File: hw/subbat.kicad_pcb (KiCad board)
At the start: 2 copper layers, 100 x 100 mm, 247 parts, among them J1 Conn_01x02, J10 Conn_01x06_Male, J11 USB_Ax2, J12 USB_Ax2, J13 USB_Ax2, J14 RJ45, J15 Conn_01x04_Male, J16 Conn_01x06_Male, J17 Conn_01x06_Male, J18 Conn_01x02, J19 USB_B_Micro, J2 Conn_01x02, J20 Conn_02x08_Odd_Even, J21 Conn_01x02, J24 Conn_01x02, J3 Conn_01x02, J4 Conn_01x02, J5 Conn_01x02, J6 Conn_01x02, J7 Conn_01x06_Male, J8 Conn_01x02, J9 USB_Ax2, Q1 Q_NPN_BEC, Q10 Q_NPN_BEC, Q11 AOD403, Q12 AOD403, Q13 Q_NPN_BEC, Q14 AOD403, Q15 Q_NPN_BEC, Q16 Q_Photo_NPN_EC, Q17 Q_NPN_BEC, Q18 Q_PNP_BEC, Q2 Q_PMOS_GSD, Q3 TPH11006NL, Q9 AOD403, SW1 SW_Push, SW2 SW_Push, SW3 SW_Push, SW4 SW_SPDT_WITH_SHIELD, SW5 SW_SPDT_WITH_SHIELD, U1 ATMEGA328P-AU, U10 P82B715, U11 TPS54202, U12 L7803, U13 TPS54202, U2 L7803, U3 ATTINY2313-20SU, U4 ATTINY13A-SSU, U5 LT6105, U6 LT6105, U7 LT6105, U8 LT6105, U9 LM393

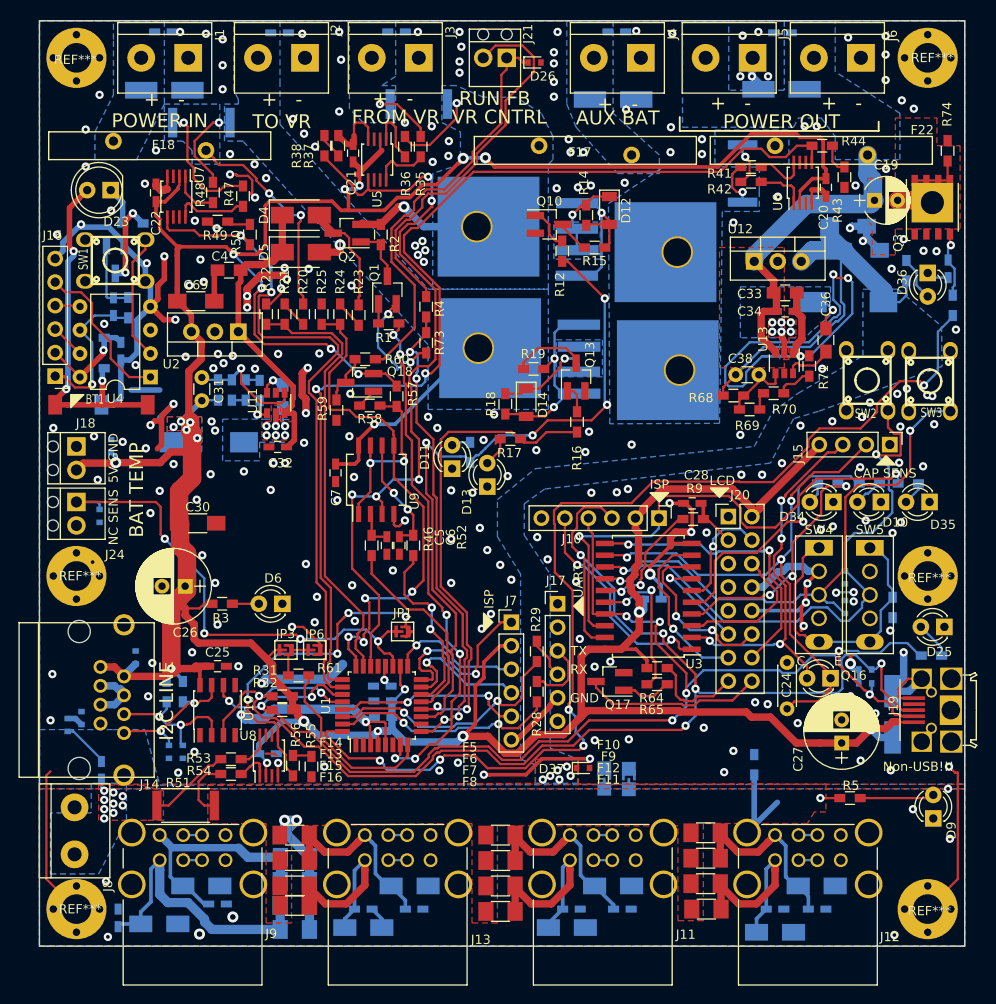
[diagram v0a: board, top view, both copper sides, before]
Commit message: some improvements; DRC clear
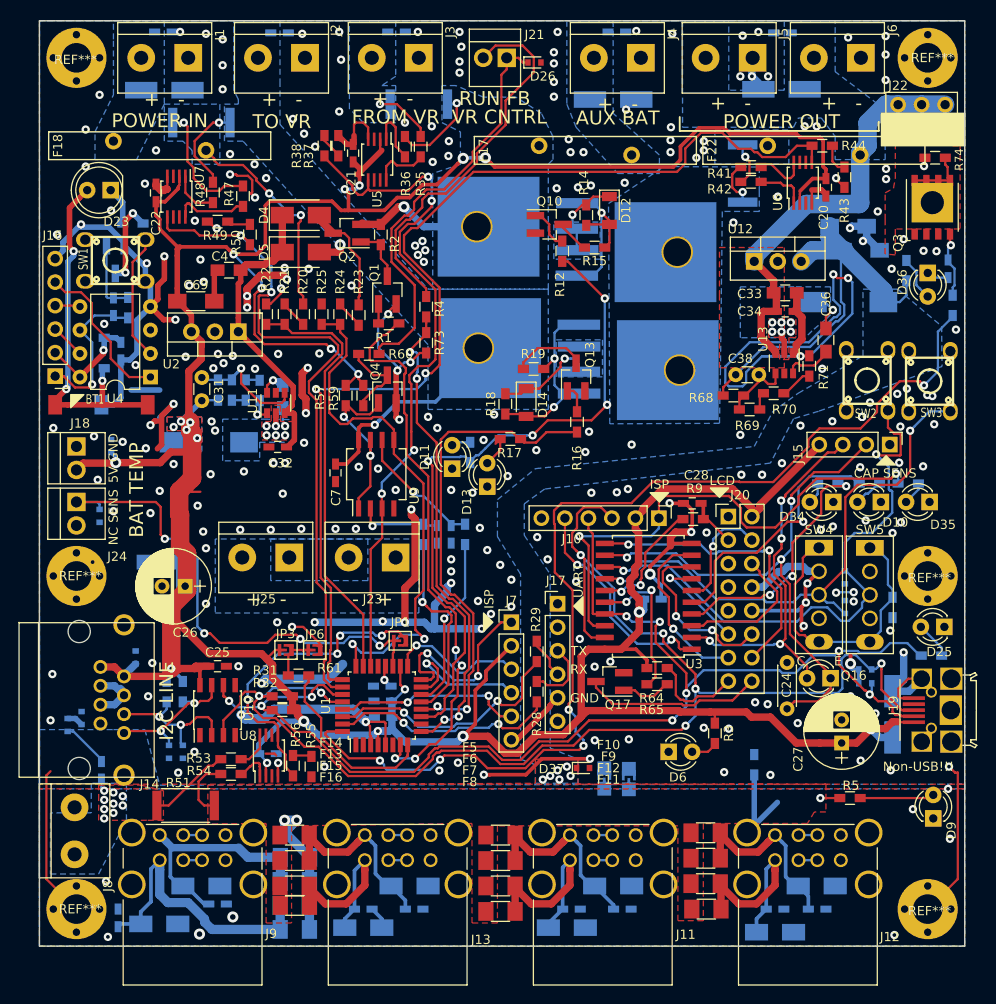
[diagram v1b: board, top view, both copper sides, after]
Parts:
- removed C19: 2200u 35V x 2, Capacitors_ThroughHole:CP_Radial_D5.0mm_P2.50mm
- removed Q18: Q_PNP_BEC, TO_SOT_Packages_SMD:SOT-23_Handsoldering
- removed R58: 10k, Resistors_SMD:R_0603_HandSoldering
- added J22: Conn_02x03_Odd_Even, Pin_Headers:Pin_Header_Straight_2x03_Pitch2.54mm, F.Cu at (112.8, 31.6)
- added J23: Conn_01x02, Terminal_Blocks:TerminalBlock_bornier-2_P5.08mm, F.Cu at (58.5, 78.0)
- added J25: Conn_01x02, Terminal_Blocks:TerminalBlock_bornier-2_P5.08mm, F.Cu at (47.0, 78.0)
- added Q4: Q_NPN_BEC, TO_SOT_Packages_SMD:SOT-23_Handsoldering, F.Cu at (57.6, 59.8)
- C30, C5, C6, R46, R52: moved to B.Cu
- J18, J21, J24: footprint components:TerminalBlock_2_P_2.54mm -> components:TerminalBlock_2_P_2.54mm_without_hole
- R57: value 22k -> 10k
- moved R3 55.1 mm to (93.0, 97.0), turned to 270 degrees
- moved D6 44.7 mm to (88.0, 99.0), turned to 0 degrees
- moved C6 5.72 mm to (64.5, 75.5)
- moved R46 5.72 mm to (61.5, 75.5)
- moved R52 5.72 mm to (66.0, 75.5)
- moved C5 5.58 mm to (63.0, 75.5)
- moved C30 5.53 mm to (33.5, 78.5), turned to 180 degrees
- moved R57 5.50 mm to (53.1, 60.5)
- moved R59 3.30 mm to (55.0, 60.5)
- moved R74 1.54 mm to (116.8, 34.8), turned to 180 degrees
- moved JP1 1.03 mm to (59.0, 87.0)
- moved F22 0.80 mm to (103.7, 34.0)
- moved R60 0.70 mm to (55.6, 56.0)
- moved U9 0.60 mm to (56.4, 69.0)
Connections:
- R59 pad 1: GND -> Net-(Q4-Pad3)
- R59 pad 2: Net-(Q18-Pad3) -> +5V
- R60 pad 1: Net-(Q18-Pad3) -> Net-(Q4-Pad3)
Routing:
- net GND: track 350.8 -> 392.9 mm, vias 247 -> 257
- net /VOUT2: track 33.9 -> 45.6 mm
- net Net-(Q4-Pad3): track 0.00 -> 9.09 mm
- net /ICHARGE_SENS: track 84.1 -> 75.7 mm, vias 5 -> 4
- net Net-(Q18-Pad3): track 5.70 -> 0.00 mm
- net Net-(C5-Pad1): track 4.07 -> 9.14 mm, vias 0 -> 1
- net /~DEEP_SLEEP_EN: track 56.6 -> 61.3 mm, vias 6 -> 4
- net /IUSB_SENS: track 38.7 -> 35.3 mm
- net /IOUT_SENS: track 114.8 -> 117.1 mm
- net Net-(Q18-Pad1): track 2.17 -> 0.00 mm
- net /VA_SENSE_ADC: track 55.2 -> 57.4 mm, vias 4 -> 2
- net /OUTCAP_N: track 12.5 -> 14.6 mm
- net +5V: track 424.3 -> 426.2 mm
- net /SW_BAT: track 74.6 -> 72.8 mm
- net Net-(C6-Pad1): track 12.7 -> 14.3 mm, vias 2 -> 1
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- added copper zone on B.Cu, net /PT_N
- added copper zone on B.Cu, net /PT_P
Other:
- board text added: "- +"

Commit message: Final Revision; PCB ordered using this version
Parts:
- added C19: 1u, Capacitors_SMD:C_0603_HandSoldering, B.Cu at (50.5, 80.8)
- added D33: ESD5Z5.0T1G, Diodes_SMD:D_SOD-523, B.Cu at (30.0, 75.4)
- added D42: ESD5Z5.0T1G, Diodes_SMD:D_SOD-523, B.Cu at (66.1, 24.0)
- added D43: 30V, Diodes_SMD:D_SMA_Handsoldering, B.Cu at (44.6, 74.6)
- added R58: 120R, Resistors_SMD:R_0603_HandSoldering, B.Cu at (27.2, 76.0)
- added R76: 1M, Resistors_SMD:R_0603_HandSoldering, B.Cu at (29.6, 82.4)
- C45: value 1u -> 1u DNI
- D26: moved to B.Cu
- R34, R40: value 2.2k -> 1k
- R74: value 10k -> 10R 2W@long, 20W@1 sec; footprint Resistors_SMD:R_0603_HandSoldering -> Resistors_SMD:R_2512; moved to B.Cu
- R75: value 100k -> 10R
- U10: value P82B715 -> P82B96
- moved J23 11.3 mm to (47.2, 78.0)
- moved J25 11.3 mm to (58.3, 78.0)
- moved D28 1.90 mm to (33.6, 99.0)
- moved R74 1.80 mm to (115.0, 34.8)
- moved D26 1.26 mm to (72.3, 24.1), turned to 270 degrees
- moved D27 1.00 mm to (35.0, 99.0)
- moved R40 0.60 mm to (34.9, 92.5)
- moved R34 0.35 mm to (33.4, 92.5)
- moved C3 0.30 mm to (57.0, 92.2)
- turned R43 to 90 degrees
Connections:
- net Net-(U1-Pad10) renamed /DIGITAL_IN1
- J14 pad 2: GND -> +5V
- J14 pad 6: GND -> +5V
- J14 pad 7: +5V -> GND
- J14 pad 8: +5V -> GND
- J14 pad 9: GND -> Net-(J14-Pad9)
- R57 pad 2: +5V -> /SW_VR
- U1 pad 1: Net-(U1-Pad1) -> /OUTCAP_CHARGE
- U1 pad 11: /SW_BAT -> /DIGITAL_IN0
- U1 pad 2: Net-(U1-Pad2) -> /SW_BAT
- U1 pad 32: /OUTCAP_CHARGE -> /DIGITAL_IN2
- U10 pad 1: (no net) -> SDA
- U10 pad 2: /SCL_L -> /SDA_L
- U10 pad 3: SCL -> /SDA_L
- U10 pad 5: (no net) -> /SCL_L
- U10 pad 6: SDA -> /SCL_L
- U10 pad 7: /SDA_L -> SCL
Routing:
- net GND: track 392.9 -> 484.8 mm, vias 257 -> 298
- net /DIGITAL_IN0: track 0.00 -> 59.3 mm, vias 0 -> 5
- net Net-(J14-Pad9): track 0.00 -> 34.4 mm
- net /ISYS_SENS: track 73.7 -> 85.4 mm
- net /IOUT_SENS: track 117.1 -> 128.6 mm
- net /SW_BAT: track 72.8 -> 83.4 mm, vias 4 -> 6
- net /SW_VR: track 52.4 -> 62.1 mm, vias 4 -> 5
- net /VS_SENSE_ADC: track 46.5 -> 55.4 mm
- net /SW_VS: track 52.3 -> 45.4 mm
- net /OUTCAP_CHARGE: track 116.9 -> 111.3 mm
- net /ICHARGE_SENS: track 75.7 -> 81.1 mm
- net /MISO: track 21.0 -> 16.8 mm
- net /SCL_L: track 16.6 -> 20.9 mm, vias 2 -> 3
- net /MOSI: track 15.3 -> 11.0 mm
- net /SDA_L: track 15.6 -> 19.6 mm
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- added copper zone on B.Cu, net /OUTCAP_N
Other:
- board text added: "+"
- board text added: "-"
- board text added: "DI0 SENS"
- board text removed: "NC SENS"

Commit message: Added annotation to date
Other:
- board text added: "10u"
- board text added: "1K"
- board text added: "3V3"
- board text added: "4.7k"
- board text added: "BiDi-SWITCH"
- board text added: "DNI"
- board text added: "SCL"
- board text added: "SDA"
- board text added: "VREF"
- board text added: "VR_IN"
- board text added: "VR_SENS_ADC"
